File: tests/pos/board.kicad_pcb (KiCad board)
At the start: 2 copper layers, 22 x 12 mm, 3 parts, among them J1 Power

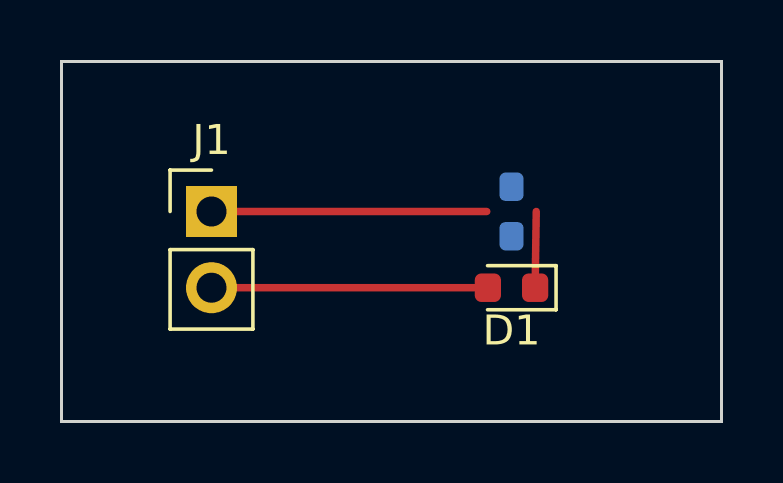
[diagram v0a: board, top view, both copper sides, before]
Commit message: fix: kicad_pos's origin, use_drill_file_origin and the exclude_th test
agy's review of PR 64 found three things.

* The doc said positions are measured from the board's origin. Without
  --use-drill-file-origin kicad-cli measures them from the top-left
  corner of the page, so the doc says that, and a new attribute,
  use_drill_file_origin, measures them from the board's drill and place
  file origin, which a pick-and-place machine usually wants.
* exclude_th had no test of its output, and on the test board it gave
  what smd_only gave. The board gains R2, a resistor with neither the
  SMD nor the through-hole attribute: smd_only drops it and exclude_th
  keeps it. The board's drill and place file origin is now its
  bottom-left corner, (100, 107), and drill_origin_test checks the
  positions measured from it.
* The analysis test now checks a name that already ends in .csv, on
  flags.csv, which also gives every flag.

The expected files are written by hand; each gains R2's row where it
belongs.

This commit has been created by an automated coding assistant,
with human supervision.

Prompt:
(Garfield, on the bus, for the operator: "Assignments for
bazel_rules_kicad (operator's request) ... @anthropic-worker-eph4.txhdl-loop1
-> https://github.com/filmil/bazel_rules_kicad/issues/24 kicad_pos")

Co-Authored-By: Claude Opus 5.5 <noreply@anthropic.com>
Claude-Session: https://claude.ai/code/session_01MDcz6bK1eTetcThu2igyHF
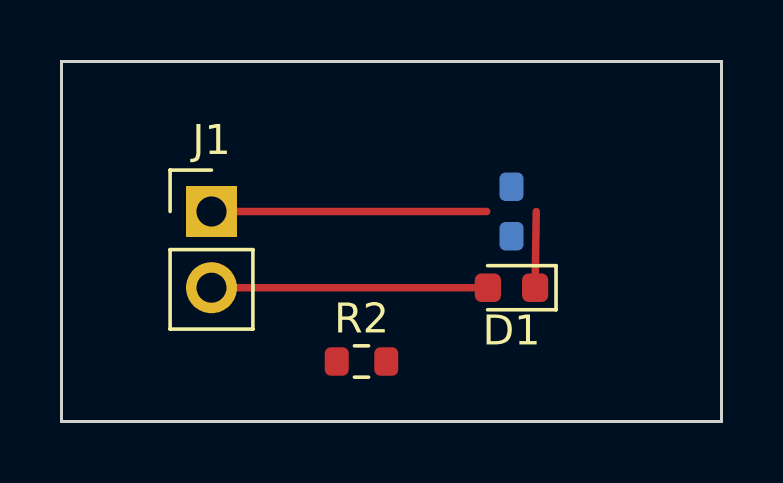
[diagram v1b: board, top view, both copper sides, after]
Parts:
- added R2: 1k, Resistor_SMD:R_0603_1608Metric, F.Cu at (110.0, 105.0)
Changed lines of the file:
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@@
 	)
 	(setup
+		(aux_axis_origin 100 107)
 		(pad_to_mask_clearance 0)
 		(allow_soldermask_bridges_in_footprints no)
@@
 			(offset
 				(xyz 0 0 0)
+			)
+			(scale
+				(xyz 1 1 1)
+			)
+			(rotate
+				(xyz 0 0 0)
+			)
+		)
+	)
+	(footprint "Resistor_SMD:R_0603_1608Metric"
+		(layer "F.Cu")
+		(at 110 105)
+		(descr "Resistor SMD 0603 (1608 Metric), square (rectangular) end terminal, IPC-7351 nominal, (Body size source: IPC-SM-782 page 72, https://www.pcb-3d.com/wordpress/wp-content/uploads/ipc-sm-782a_amendment_1_and_2.pdf), generated with kicad-footprint-generator")
+		(tags "resistor")
+		(property "Reference" "R2"
+			(at 0 -1.43 0)
+			(layer "F.SilkS")
+			(effects
+				(font
+					(size 1 1)
+					(thickness 0.15)
+				)
+			)
+		)
+		(property "Value" "1k"
+			(at 0 1.43 0)
+			(layer "F.Fab")
+			(effects
+				(font
+					(size 1 1)
+					(thickness 0.15)
+				)
+			)
+		)
+		(property "Datasheet" ""
+			(at 0 0 0)
+			(layer "F.Fab")
+			(hide yes)
+			(effects
+				(font
+					(size 1.27 1.27)
+					(thickness 0.15)
+				)
+			)
+		)
+		(property "Description" ""
+			(at 0 0 0)
+			(layer "F.Fab")
+			(hide yes)
+			(effects
+				(font
+					(size 1.27 1.27)
+					(thickness 0.15)
+				)
+			)
+		)
+		(fp_line
+			(start -0.237258 -0.5225)
+			(end 0.237258 -0.5225)
+			(stroke
+				(width 0.12)
+				(type solid)
+			)
+			(layer "F.SilkS")
+		)
+		(fp_line
+			(start -0.237258 0.5225)
+			(end 0.237258 0.5225)
+			(stroke
+				(width 0.12)
+				(type solid)
+			)
+			(layer "F.SilkS")
+		)
+		(fp_rect
+			(start -1.48 -0.73)
+			(end 1.48 0.73)
+			(stroke
+				(width 0.05)
+				(type solid)
+			)
+			(fill no)
+			(layer "F.CrtYd")
+		)
+		(fp_rect
+			(start -0.8 -0.4125)
+			(end 0.8 0.4125)
+			(stroke
+				(width 0.1)
+				(type solid)
+			)
+			(fill no)
+			(layer "F.Fab")
+		)
+		(fp_text user "${REFERENCE}"
+			(at 0 0 0)
+			(layer "F.Fab")
+			(effects
+				(font
+					(size 0.4 0.4)
+					(thickness 0.06)
+				)
+			)
+		)
+		(pad "1" smd roundrect
+			(at -0.825 0)
+			(size 0.8 0.95)
+			(layers "F.Cu" "F.Mask" "F.Paste")
+			(roundrect_rratio 0.25)
+		)
+		(pad "2" smd roundrect
+			(at 0.825 0)
+			(size 0.8 0.95)
+			(layers "F.Cu" "F.Mask" "F.Paste")
+			(roundrect_rratio 0.25)
+		)
+		(embedded_fonts no)
+		(model "${KICAD9_3DMODEL_DIR}/Resistor_SMD.3dshapes/R_0603_1608Metric.step"
+			(offset
+				(xyz 0 0 0)
